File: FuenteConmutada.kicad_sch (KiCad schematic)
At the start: 0 parts

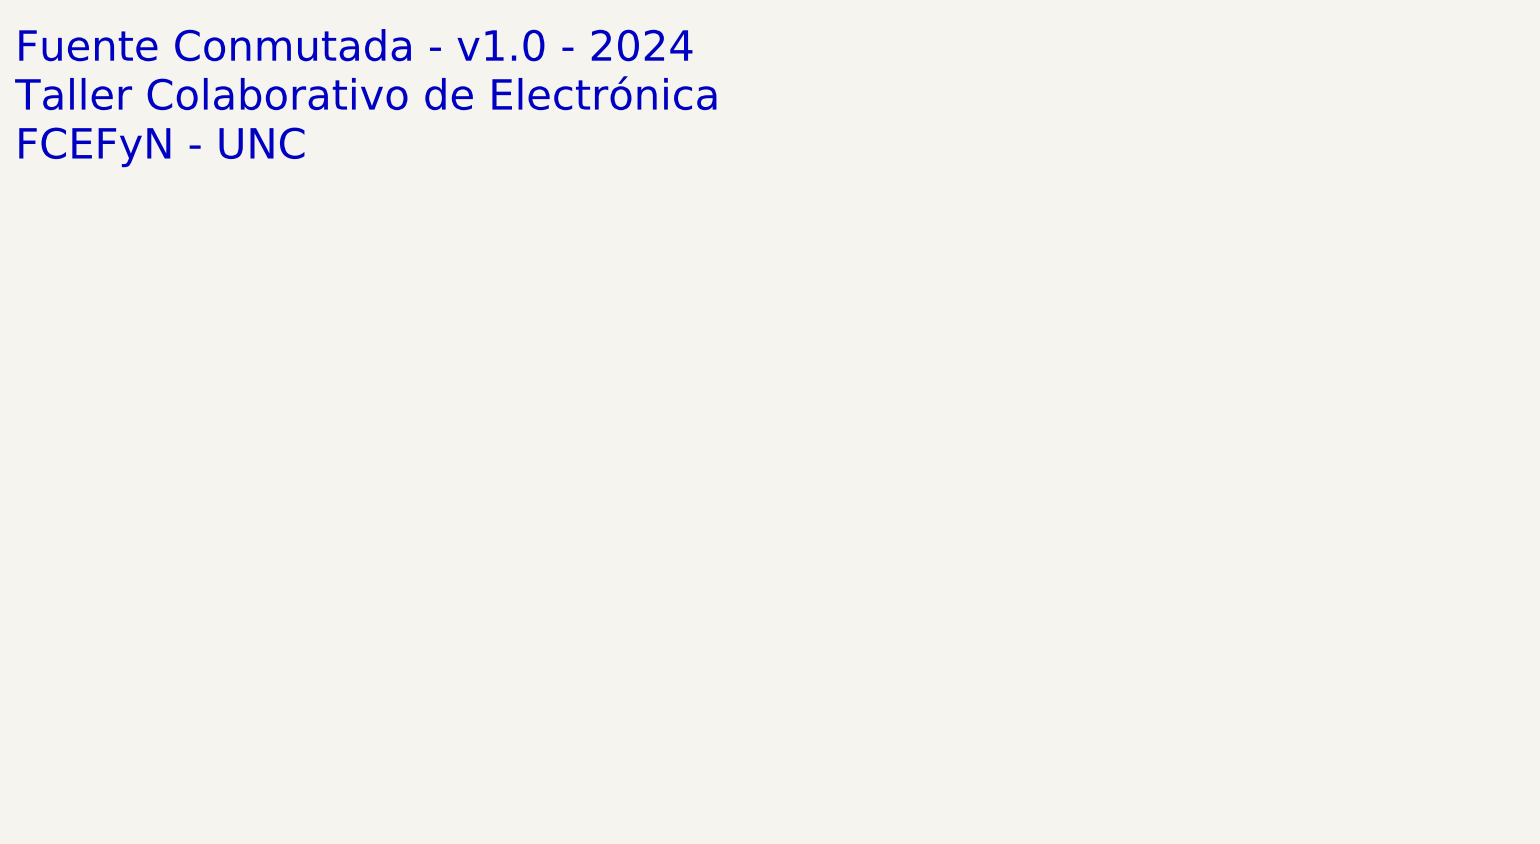
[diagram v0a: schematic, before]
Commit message: Simulación en PSpice + esquemático
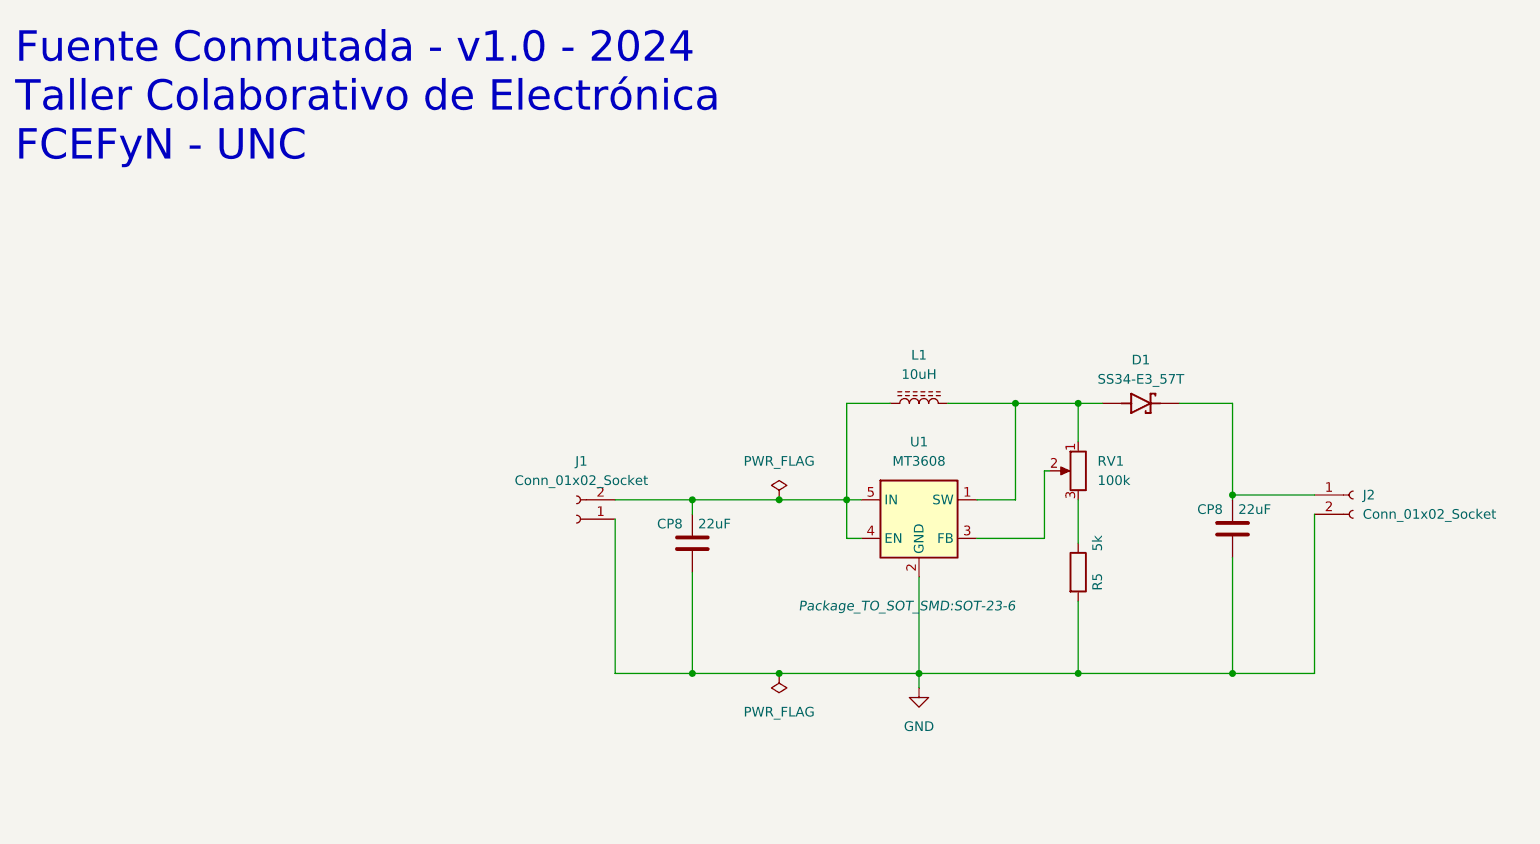
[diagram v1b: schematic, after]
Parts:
- added CP8 (x2): 22uF, Capacitor_SMD:C_1206_3216Metric_Pad1.33x1.80mm_HandSolder, symbol Device:C
- added D1: SS34-E3_57T, Diode_SMD:D_SMC_Handsoldering, symbol SS34-E3_57T:SS34-E3_57T
- added J1, J2: Conn_01x02_Socket, Connector_PinSocket_2.54mm:PinSocket_1x02_P2.54mm_Vertical, symbol Connector:Conn_01x02_Socket
- added L1: 10uH, Inductor_SMD:L_Taiyo-Yuden_NR-80xx_HandSoldering, symbol Device:L_Ferrite
- added R5: 5k, Resistor_SMD:R_1206_3216Metric_Pad1.30x1.75mm_HandSolder, symbol Device:R
- added RV1: 100k, Potentiometer_THT:Potentiometer_Bourns_3299W_Vertical, symbol Device:R_Potentiometer
- added U1: MT3608, Package_TO_SOT_SMD:SOT-23-6, symbol Regulator_Switching:MT3608
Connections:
- new net: CP8.2, D1.C, J2.1 (Pin_1)
- new net: D1.A, L1.2, RV1.1, U1.1 (SW)
- new net: RV1.2, U1.3 (FB)
- new net: CP8.2, J1.2 (Pin_2), L1.1, U1.4 (EN), U1.5 (IN)
- new net: R5.1, RV1.3
- new net GND: CP8.1, CP8.1, J1.1 (Pin_1), J2.2 (Pin_2), R5.2, U1.2 (GND)

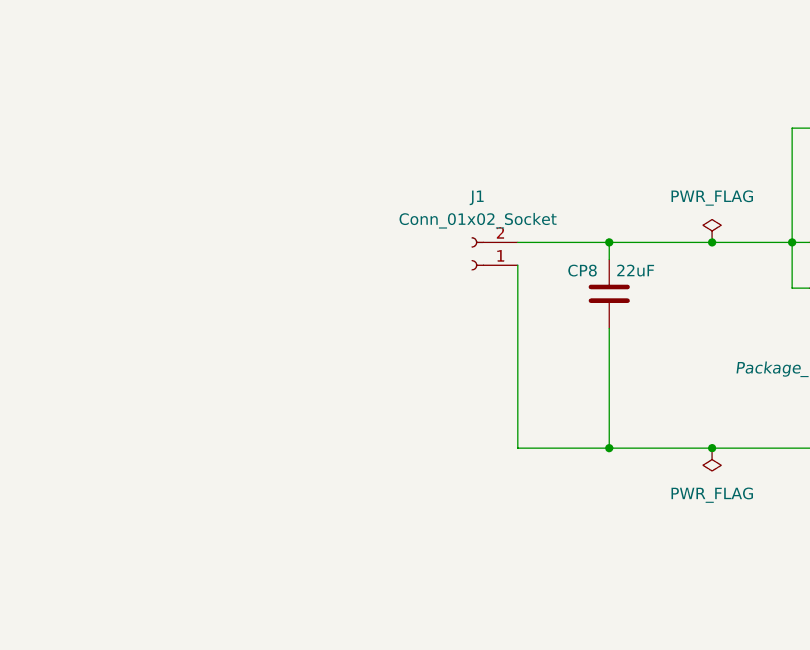
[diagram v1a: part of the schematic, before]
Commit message: USB C de entrada
Revisar huella para no cometer el mismo error que en la placa del PIC
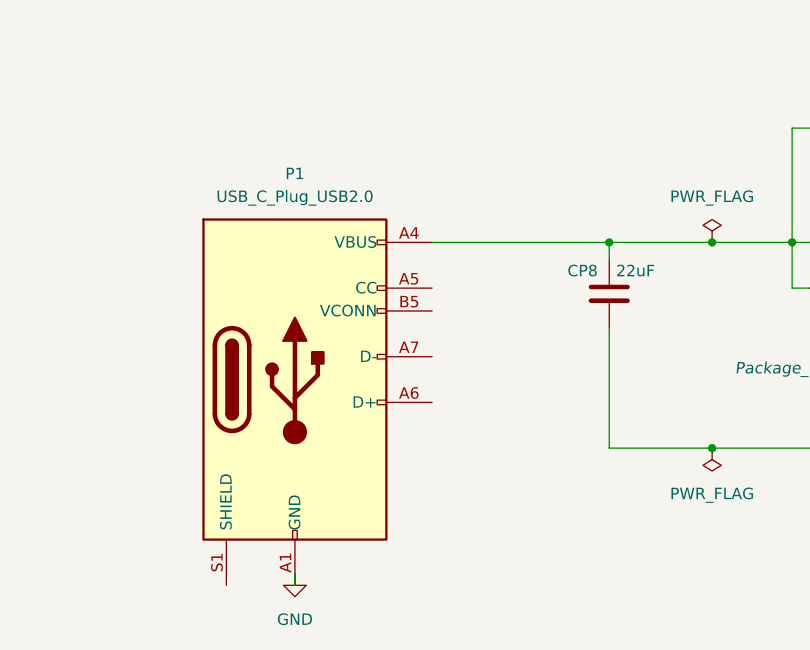
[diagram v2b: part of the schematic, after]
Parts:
- removed J1: Conn_01x02_Socket, Connector_PinSocket_2.54mm:PinSocket_1x02_P2.54mm_Vertical, symbol Connector:Conn_01x02_Socket
- added P1: USB_C_Plug_USB2.0, Connector_USB:USB_C_Receptacle_GCT_USB4105-xx-A_16P_TopMnt_Horizontal, symbol Connector:USB_C_Plug_USB2.0
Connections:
- net GND: now also P1.A1 (GND), P1.A12 (GND), P1.B1 (GND), P1.B12 (GND)
- net at CP8.2, L1.1, U1.4 (EN)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: now also P1.A4 (VBUS), P1.A9 (VBUS), P1.B4 (VBUS), P1.B9 (VBUS)
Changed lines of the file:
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@@
   (junction (at 125.73 76.2) (diameter 0) (color 0 0 0 0)
   )
-  (junction (at 105.41 99.06) (diameter 0) (color 0 0 0 0)
-  )
   (junction (at 116.84 99.06) (diameter 0) (color 0 0 0 0)
   )
@@
     (stroke (width 0) (type default))
   )
-  (wire (pts (xy 95.25 76.2) (xy 105.41 76.2))
+  (wire (pts (xy 85.725 76.2) (xy 105.41 76.2))
     (stroke (width 0) (type default))
   )
@@
     (stroke (width 0) (type default))
   )
-  (wire (pts (xy 95.25 99.06) (xy 105.41 99.06))
-    (stroke (width 0) (type default))
-  )
   (wire (pts (xy 151.765 72.39) (xy 151.765 81.28))
     (stroke (width 0) (type default))
@@
     (stroke (width 0) (type default))
   )
-  (wire (pts (xy 95.25 78.74) (xy 95.25 99.06))
-    (stroke (width 0) (type default))
-  )
   (wire (pts (xy 116.84 99.06) (xy 135.255 99.06))
     (stroke (width 0) (type default))
   )
   (wire (pts (xy 176.53 75.565) (xy 176.53 76.2))
+    (stroke (width 0) (type default))
+  )
+  (wire (pts (xy 70.485 114.3) (xy 70.485 113.03))
     (stroke (width 0) (type default))
   )
@@
     )
   )
+  (symbol (lib_id "Connector:USB_C_Plug_USB2.0") (at 70.485 91.44 0) (unit 1)
+    (in_bom yes) (on_board yes) (dnp no) (fields_autoplaced)
+    (property "Reference" "P1" (at 70.485 68.58 0)
+      (effects (font (size 1.27 1.27)))
+    )
+    (property "Value" "USB_C_Plug_USB2.0" (at 70.485 71.12 0)
+      (effects (font (size 1.27 1.27)))
+    )
+    (property "Footprint" "Connector_USB:USB_C_Receptacle_GCT_USB4105-xx-A_16P_TopMnt_Horizontal" (at 74.295 91.44 0)
+      (effects (font (size 1.27 1.27)) hide)
+    )
+    (property "Datasheet" "https://www.usb.org/sites/default/files/documents/usb_type-c.zip" (at 74.295 91.44 0)
+      (effects (font (size 1.27 1.27)) hide)
+    )
+    (pin "A1")
+    (pin "A12")
+    (pin "A4")
+    (pin "A5")
+    (pin "A6")
+    (pin "A7")
+    (pin "A9")
+    (pin "B1")
+    (pin "B12")
+    (pin "B4")
+    (pin "B5")
+    (pin "B9")
+    (pin "S1")
+    (instances
+      (project "PIC16F887EV"
+        (path "/a2515825-f12e-4570-8718-6acb93c561c0"
+          (reference "P1") (unit 1)
+        )
+      )
+      (project "FuenteConmutada"
+        (path "/d7444c1b-87b0-4ff7-a57a-a32071ba4b64"
+          (reference "P1") (unit 1)
+        )
+      )
+    )
+  )
+  (symbol (lib_id "power:GND") (at 70.485 113.03 0) (unit 1)
+    (in_bom yes) (on_board yes) (dnp no) (fields_autoplaced)
+    (property "Reference" "#PWR02" (at 70.485 119.38 0)
+      (effects (font (size 1.27 1.27)) hide)
+    )
+    (property "Value" "GND" (at 70.485 118.11 0)
+      (effects (font (size 1.27 1.27)))
+    )
+    (property "Footprint" "" (at 70.485 113.03 0)
+      (effects (font (size 1.27 1.27)) hide)
+    )
+    (property "Datasheet" "" (at 70.485 113.03 0)
+      (effects (font (size 1.27 1.27)) hide)
+    )
+    (pin "1")
+    (instances
+      (project "FuenteConmutada"
+        (path "/d7444c1b-87b0-4ff7-a57a-a32071ba4b64"
+          (reference "#PWR02") (unit 1)
+        )
+      )
+    )
+  )
   (symbol (lib_id "power:PWR_FLAG") (at 116.84 99.06 180) (unit 1)
     (in_bom yes) (on_board yes) (dnp no) (fields_autoplaced)
@@
         )
       )
-    )
-  )
-  (symbol (lib_id "Connector:Conn_01x02_Socket") (at 90.17 78.74 180) (unit 1)
-    (in_bom yes) (on_board yes) (dnp no) (fields_autoplaced)
-    (property "Reference" "J1" (at 90.805 71.12 0)
-      (effects (font (size 1.27 1.27)))
-    )
-    (property "Value" "Conn_01x02_Socket" (at 90.805 73.66 0)
-      (effects (font (size 1.27 1.27)))
-    )
-    (property "Footprint" "Connector_PinSocket_2.54mm:PinSocket_1x02_P2.54mm_Vertical" (at 90.17 78.74 0)
-      (effects (font (size 1.27 1.27)) hide)
-    )
-    (property "Datasheet" "~" (at 90.17 78.74 0)
-      (effects (font (size 1.27 1.27)) hide)
-    )
-    (pin "1")
-    (pin "2")
-    (instances
-      (project "FuenteConmutada"
-        (path "/d7444c1b-87b0-4ff7-a57a-a32071ba4b64"
-          (reference "J1") (unit 1)
-        )
-      )
